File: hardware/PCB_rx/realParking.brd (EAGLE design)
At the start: 100 x 80 mm, 14 parts, among them IC1 MEGA8-P, IC2 LD117AV

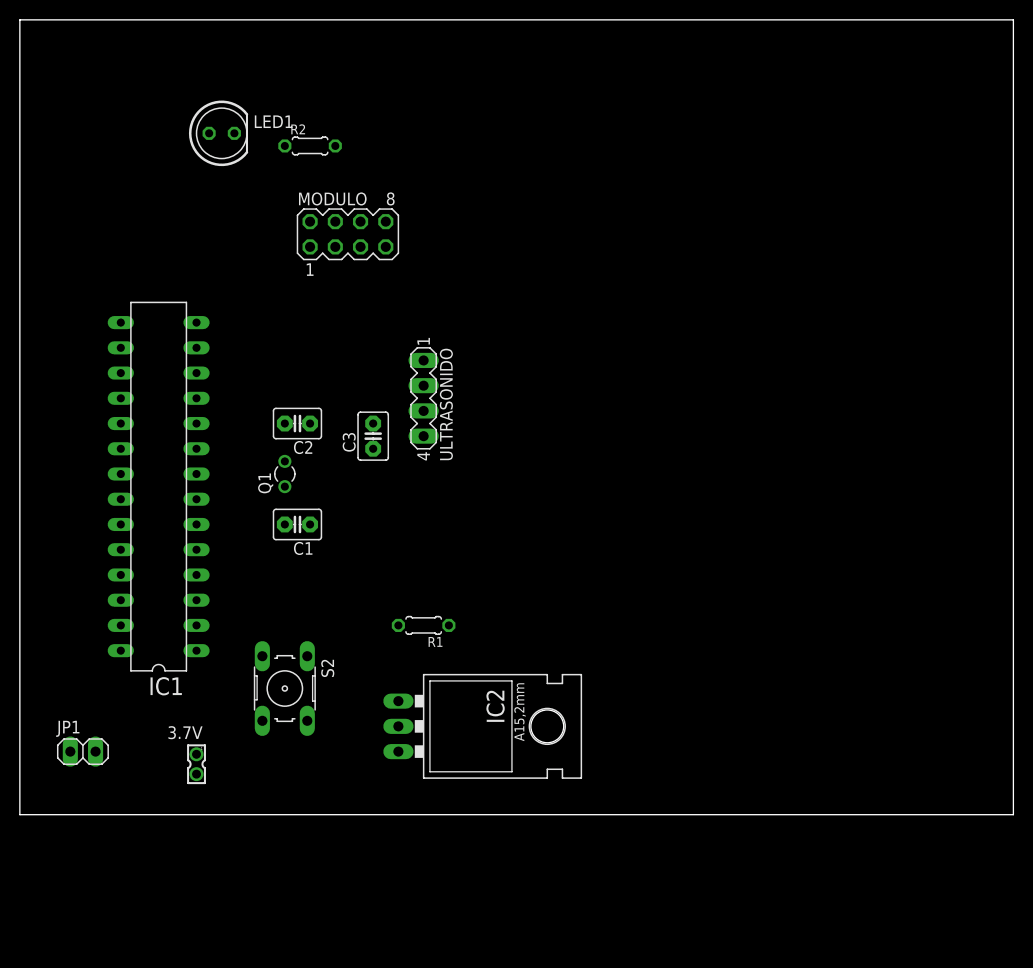
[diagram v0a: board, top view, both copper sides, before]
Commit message: Se arregla diseño PCB del modulo transmisor
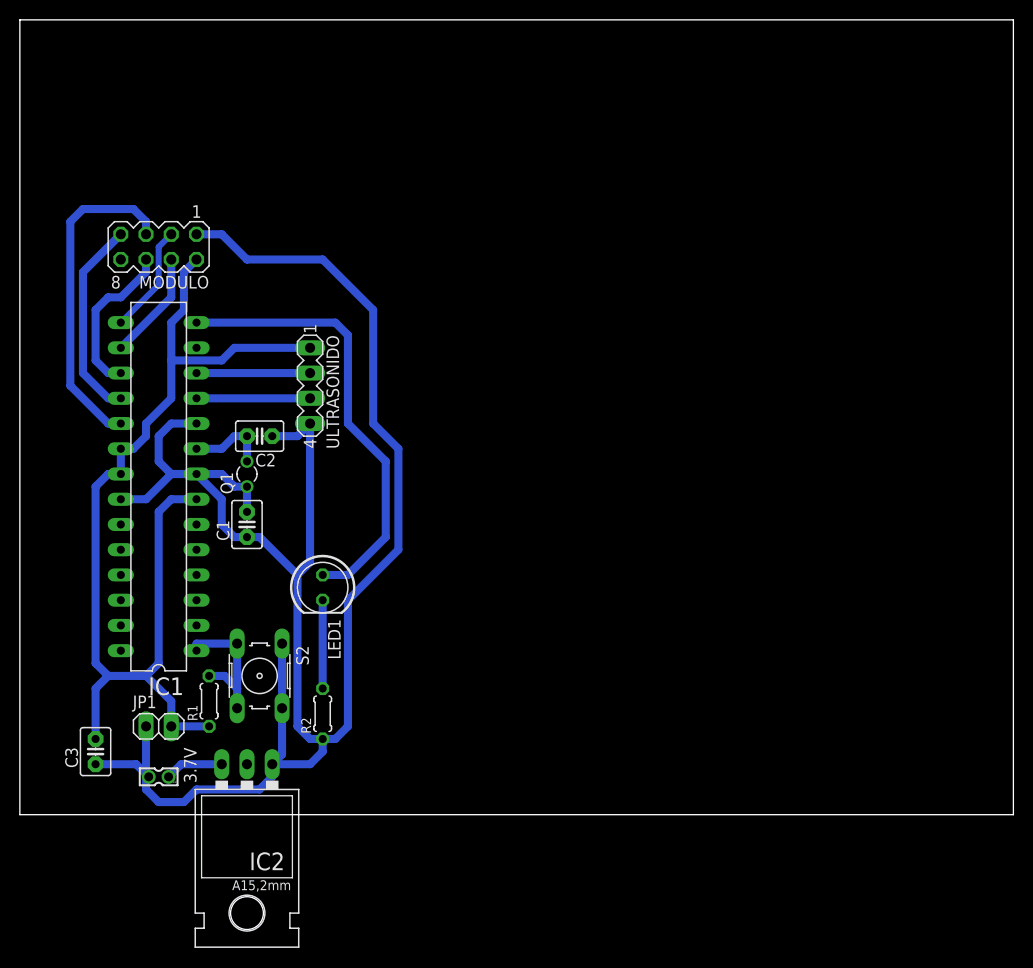
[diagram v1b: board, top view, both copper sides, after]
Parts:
- moved R2 57.2 mm to (30.5, 10.2), turned to 90 degrees
- moved LED1 46.8 mm to (30.5, 22.9), turned to 270 degrees
- moved C3 42.3 mm to (7.62, 6.35)
- moved R1 22.9 mm to (19.1, 11.4), turned to 90 degrees
- moved IC2 20.5 mm to (22.9, 1.27), turned to 180 degrees
- moved MODULO 19.1 mm to (14.0, 57.1), turned to 180 degrees
- moved ULTRASONIDO 11.5 mm to (29.2, 43.2)
- moved JP1 8.03 mm to (14.0, 8.89)
- moved C1 5.08 mm to (22.9, 29.2), turned to 90 degrees
- moved 3.7V 4.02 mm to (14.0, 3.81), turned to 90 degrees
- moved C2 4.02 mm to (24.1, 38.1)
- moved Q1 3.81 mm to (22.9, 34.3)
- moved S2 2.84 mm to (24.1, 14.0)
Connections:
- removed net N$5: ULTRASONIDO.1
- removed net N$7: MODULO.2
- net 3.3V: now also C3.2, MODULO.2, ULTRASONIDO.1; no longer C3.1
- net GND: now also C3.1; no longer C3.2
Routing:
- net GND: track 0.00 -> 179.6 mm
- net 3.3V: track 0.00 -> 104.6 mm
- net N$8: track 0.00 -> 45.6 mm
- net N$13: track 0.00 -> 33.1 mm
- net N$12: track 0.00 -> 20.4 mm
- net N$15: track 0.00 -> 19.4 mm
- net N$11: track 0.00 -> 16.1 mm
- net N$16: track 0.00 -> 14.6 mm
- net N$4: track 0.00 -> 11.4 mm
- net N$3: track 0.00 -> 11.4 mm
- net N$10: track 0.00 -> 11.0 mm
- net N$9: track 0.00 -> 11.0 mm
- net N$6: track 0.00 -> 8.89 mm
- net N$14: track 0.00 -> 8.15 mm
- net N$2: track 0.00 -> 5.88 mm
